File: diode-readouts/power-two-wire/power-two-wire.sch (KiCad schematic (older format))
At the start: 10 parts, among them J1 JST_SH_Conn_01x04_i2c_horizon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, J2 JST_SH_Conn_01x04_i2c_horizon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, J3 JST_SH_Conn_01x04_i2c_horizon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, J6 JST_SH_Conn_01x04_i2c_horizon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, J7 Conn_01x06_SPI, J8 Conn_01x06_Female

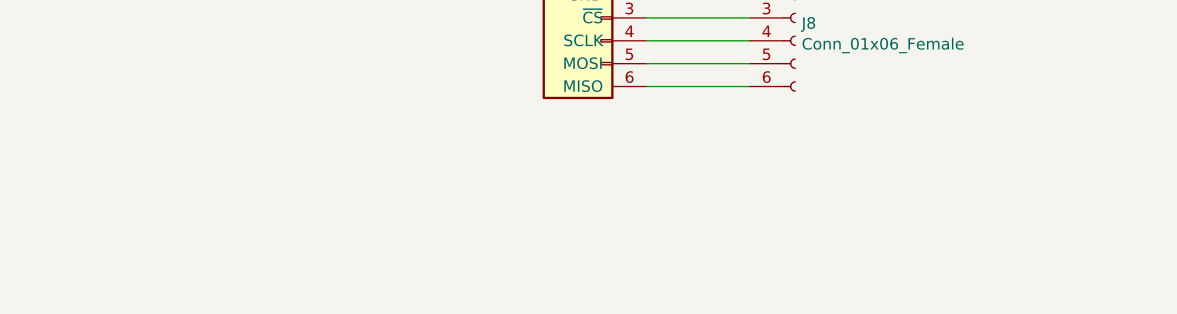
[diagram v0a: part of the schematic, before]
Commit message: add uart mux versions
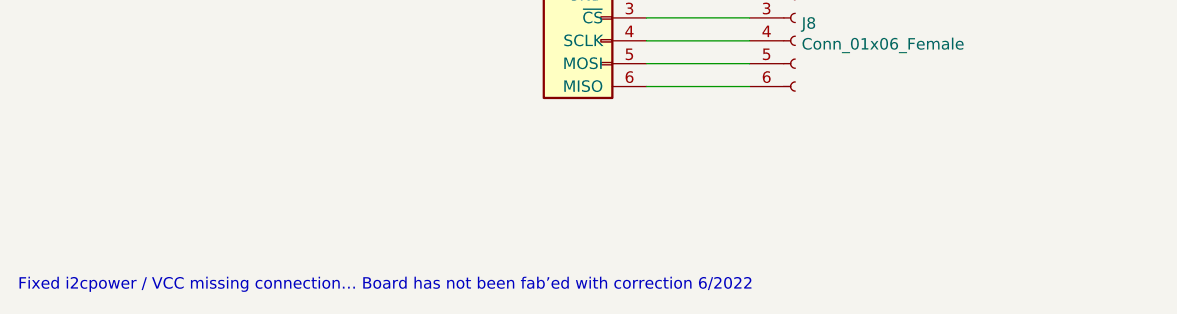
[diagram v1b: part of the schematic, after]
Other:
- note added: "Fixed i2cpower / VCC missing connection… Board has not been fab’ed with correction 6/2022"
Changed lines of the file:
@@
 Wire Wire Line
 	5350 5800 4900 5800
+Text Notes 2150 6700 0    50   ~ 0
+Fixed i2cpower / VCC missing connection… Board has not been fab’ed with correction 6/2022
 $EndSCHEMATC
